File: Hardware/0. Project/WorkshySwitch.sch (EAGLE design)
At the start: 52 parts, among them IC1 LM1117-3.3, K1 G3MB-202P, Q3 32-MHz, Q4 32.768-kHz, T1 BC848, U2 HLK-PM01, U3 CC2541

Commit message: PCB layout under dev
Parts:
- removed F1: SF70E, Thermal Fuse:LITTLEFUSE
- removed IC1: LM1117-3.3, v-reg:LD117AS33TR
- added F3: SF70E, fuse:LITTLEFUSE
- added U1: LM1117-3.3, REG1117:REG1117
- X1: device con-ptr500:AK500/2-H -> con-ptr500:AK500/2
- X3: device con-ptr500:AK500/3-H -> con-ptr500:AK500/3
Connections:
- net 3.3V: now also U1.VOUT; no longer IC1.OUT
- net 5V: now also U1.VIN; no longer IC1.IN
- net GND: now also U1.GND; no longer IC1.ADJ
- net N$4: now also F3.2; no longer F1.1
- net N$9: now also F3.1; no longer F1.2
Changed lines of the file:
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@@
 <part name="GND8" library="supply1" library_urn="urn:adsk.eagle:library:371" deviceset="GND" device=""/>
 <part name="K1" library="G3MB202PDC12" deviceset="G3MB202PDC12" device="" value="G3MB-202P"/>
-<part name="IC1" library="v-reg" library_urn="urn:adsk.eagle:library:409" deviceset="LD117A?*" device="S" package3d_urn="urn:adsk.eagle:package:30370/1" technology="33TR" value="LM1117-3.3"/>
 <part name="SUPPLY8" library="supply2" library_urn="urn:adsk.eagle:library:372" deviceset="+4.1V" device="" value="5V"/>
 <part name="SUPPLY9" library="supply2" library_urn="urn:adsk.eagle:library:372" deviceset="+4.1V" device="" value="5V"/>
@@
 <part name="R4" library="rcl" library_urn="urn:adsk.eagle:library:334" deviceset="R-EU_" device="R0603" package3d_urn="urn:adsk.eagle:package:23555/3" value="1k"/>
 <part name="GND9" library="supply1" library_urn="urn:adsk.eagle:library:371" deviceset="GND" device=""/>
-<part name="X1" library="con-ptr500" library_urn="urn:adsk.eagle:library:181" deviceset="AK500/2-H" device="" package3d_urn="urn:adsk.eagle:package:9901/1"/>
+<part name="X1" library="con-ptr500" library_urn="urn:adsk.eagle:library:181" deviceset="AK500/2" device="" package3d_urn="urn:adsk.eagle:package:9880/1"/>
 <part name="GND10" library="supply1" library_urn="urn:adsk.eagle:library:371" deviceset="GND" device=""/>
 <part name="SUPPLY10" library="supply2" library_urn="urn:adsk.eagle:library:372" deviceset="+4.1V" device="" value="3.3V"/>
 <part name="F2" library="fuse" library_urn="urn:adsk.eagle:library:233" deviceset="QPL" device="" package3d_urn="urn:adsk.eagle:package:14085/1" value="200 mA"/>
-<part name="F1" library="Thermal Fuse" deviceset="LITTLEFUSE" device="" package3d_urn="urn:adsk.eagle:package:14064/1" value="SF70E"/>
 <part name="R5" library="varistor" library_urn="urn:adsk.eagle:library:410" deviceset="VARISTOR" device="S05K11" package3d_urn="urn:adsk.eagle:package:30524/1" value="130VRMS"/>
 <part name="C18" library="smd-ipc" library_urn="urn:adsk.eagle:library:361" deviceset="C0402" device="" value="18pF"/>
@@
 <part name="R2" library="smd-ipc" library_urn="urn:adsk.eagle:library:361" deviceset="R0402" device="" value="10k"/>
 <part name="R7" library="smd-ipc" library_urn="urn:adsk.eagle:library:361" deviceset="R0402" device="" value="10k"/>
-<part name="X3" library="con-ptr500" library_urn="urn:adsk.eagle:library:181" deviceset="AK500/3-H" device="" package3d_urn="urn:adsk.eagle:package:9899/1"/>
+<part name="X3" library="con-ptr500" library_urn="urn:adsk.eagle:library:181" deviceset="AK500/3" device="" package3d_urn="urn:adsk.eagle:package:9883/1"/>
+<part name="F3" library="fuse" deviceset="LITTLEFUSE" device="" package3d_urn="urn:adsk.eagle:package:14064/1" value="SF70E"/>
+<part name="U1" library="REG1117" deviceset="REG1117" device="" value="LM1117-3.3"/>
 </parts>
 <sheets>
@@
 <attribute name="VALUE" x="368.90725" y="175.874490625" size="1.274740625" layer="96"/>
 </instance>
-<instance part="IC1" gate="G$1" x="115.57" y="238.76" smashed="yes">
-<attribute name="NAME" x="110.49" y="245.11" size="1.778" layer="95"/>
-<attribute name="VALUE" x="110.49" y="242.57" size="1.4224" layer="96"/>
-</instance>
 <instance part="SUPPLY8" gate="P" x="102.87" y="243.84" smashed="yes">
 <attribute name="VALUE" x="100.965" y="247.015" size="1.778" layer="96"/>
@@
 <attribute name="NAME" x="38.1" y="242.697" size="1.778" layer="95" rot="MR0"/>
 <attribute name="VALUE" x="38.1" y="240.284" size="1.778" layer="96" rot="MR0"/>
-</instance>
-<instance part="F1" gate="A" x="46.99" y="238.76" smashed="yes" rot="MR0">
-<attribute name="NAME" x="50.8" y="242.697" size="1.778" layer="95" rot="MR0"/>
-<attribute name="VALUE" x="50.8" y="240.284" size="1.778" layer="96" rot="MR0"/>
 </instance>
 <instance part="R5" gate="G$1" x="59.69" y="233.68" smashed="yes" rot="MR90">
@@
 <attribute name="NAME" x="387.35" y="162.941" size="1.778" layer="95"/>
 <attribute name="VALUE" x="389.89" y="167.513" size="1.778" layer="96" rot="R180"/>
+</instance>
+<instance part="F3" gate="A" x="46.99" y="238.76" smashed="yes">
+<attribute name="NAME" x="43.18" y="240.157" size="1.778" layer="95"/>
+<attribute name="VALUE" x="43.18" y="235.839" size="1.778" layer="96"/>
+</instance>
+<instance part="U1" gate="G$1" x="115.57" y="237.49" smashed="yes">
+<attribute name="NAME" x="109.218809375" y="244.475890625" size="1.77828125" layer="95" ratio="10"/>
+<attribute name="VALUE" x="109.212090625" y="241.93895" size="1.778" layer="96" ratio="10"/>
 </instance>
 </instances>
@@
 <wire x1="128.27" y1="229.87" x2="128.27" y2="228.6" width="0.1524" layer="91"/>
 <junction x="128.27" y="228.6"/>
-<pinref part="IC1" gate="G$1" pin="ADJ"/>
 <wire x1="115.57" y1="231.14" x2="115.57" y2="228.6" width="0.1524" layer="91"/>
 <junction x="115.57" y="228.6"/>
@@
 <wire x1="92.71" y1="229.87" x2="92.71" y2="228.6" width="0.1524" layer="91"/>
 <junction x="92.71" y="228.6"/>
+<pinref part="U1" gate="G$1" pin="GND"/>
 </segment>
 <segment>
@@
 <net name="3.3V" class="0">
 <segment>
-<pinref part="IC1" gate="G$1" pin="OUT"/>
 <wire x1="128.27" y1="238.76" x2="128.27" y2="237.49" width="0.1524" layer="91"/>
-<wire x1="123.19" y1="238.76" x2="128.27" y2="238.76" width="0.1524" layer="91"/>
 <junction x="128.27" y="238.76"/>
 <pinref part="C1" gate="G$1" pin="1"/>
 <pinref part="C2" gate="G$1" pin="1"/>
+<wire x1="127" y1="238.76" x2="128.27" y2="238.76" width="0.1524" layer="91"/>
 <wire x1="138.43" y1="237.49" x2="138.43" y2="238.76" width="0.1524" layer="91"/>
 <wire x1="138.43" y1="238.76" x2="128.27" y2="238.76" width="0.1524" layer="91"/>
@@
 <wire x1="140.97" y1="238.76" x2="138.43" y2="238.76" width="0.1524" layer="91"/>
 <junction x="138.43" y="238.76"/>
+<pinref part="U1" gate="G$1" pin="VOUT"/>
 </segment>
 </net>
@@
 <pinref part="SUPPLY8" gate="P" pin="+4.1V"/>
 <wire x1="102.87" y1="241.3" x2="102.87" y2="238.76" width="0.1524" layer="91"/>
-<pinref part="IC1" gate="G$1" pin="IN"/>
 <wire x1="102.87" y1="238.76" x2="102.87" y2="237.49" width="0.1524" layer="91"/>
-<wire x1="107.95" y1="238.76" x2="102.87" y2="238.76" width="0.1524" layer="91"/>
 <pinref part="U2" gate="G$1" pin="VO+"/>
+<wire x1="104.14" y1="238.76" x2="102.87" y2="238.76" width="0.1524" layer="91"/>
 <wire x1="87.63" y1="238.76" x2="92.71" y2="238.76" width="0.1524" layer="91"/>
 <junction x="102.87" y="238.76"/>
@@
 <wire x1="92.71" y1="237.49" x2="92.71" y2="238.76" width="0.1524" layer="91"/>
 <junction x="92.71" y="238.76"/>
+<pinref part="U1" gate="G$1" pin="VIN"/>
 </segment>
 <segment>
@@
 <wire x1="52.07" y1="238.76" x2="59.69" y2="238.76" width="0.1524" layer="91"/>
 <wire x1="59.69" y1="238.76" x2="62.23" y2="238.76" width="0.1524" layer="91"/>
-<pinref part="F1" gate="A" pin="1"/>
+<pinref part="F3" gate="A" pin="2"/>
 </segment>
 </net>
 <net name="N$9" class="0">
 <segment>
-<pinref part="F1" gate="A" pin="2"/>
 <wire x1="39.37" y1="238.76" x2="41.91" y2="238.76" width="0.1524" layer="91"/>
 <pinref part="F2" gate="G$1" pin="1"/>
-</segment>
-</net>
+<pinref part="F3" gate="A" pin="1"/>
+</segment>
+</net>

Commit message: PCB layout done
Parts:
- removed JP2: (no value), pinhead:PINHD-2X5
- removed R3: 10k, rcl:R-EU_R0603
- removed S1: DTSM-3, switch-tact:DTSM-3
- added J1: ICSP, SHF-105-01-X-D-SM:SHF-105-01-X-D-SM
- added R1: R0402, smd-ipc:R0402
- added S2: 434121050816, Push Button:434121050816
- C1, C7: value 100nF -> (none)
- C18, C19: value 18pF -> C0402
- C2, C5: value 10uF -> (none)
- C21, C22, C24: value 1pF -> C0402
- C23: value DNM -> C0402
- C25: value 220pF -> C0402
- C26, C28, C29, C30, C31: value 100nF -> C0402
- C27, C32: value 1uF -> C0402
- C33, C34: value 12pF -> C0402
- C35, C36: value 15pF -> C0402
- C6: value 2.2uF -> C0402
- C9: value 100n -> C0402
- L1, L2: value 2nH -> L0402
- L3: value 1nH -> L0402
- L4: value 3nH -> L0402
- L5: value BLM15HG102SN1D -> L0402
- Q3: value 32-MHz -> FA-128
- Q4: value 32.768-kHz -> (none)
- R10: value 56k -> R0402
- R2, R7: value 10k -> R0402
- R4: value 1k -> R0402; device rcl:R-EU_R0603 -> smd-ipc:R0402
- R8: value 2.7k -> R0402
- U1: value LM1117-3.3 -> REG1117
- U3: value CC2541 -> CC2541F256RHAT
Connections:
- removed net +4.1V: C25.1, C26.1, C28.1, C29.1, C30.1, C31.1, C32.1, C6.1, JP2.2, L5.1, R2.2, R7.2, SJ1.2, U3.AVDD1, U3.AVDD2, U3.AVDD3, U3.AVDD4, U3.AVDD5, U3.AVDD6, U3.DVDD1, U3.DVDD2
- new net 3.3: C1.1, C2.1, L5.2, U1.VOUT
- net 3.3V: now also C25.1, C26.1, C28.1, C29.1, C30.1, C31.1, C32.1, C6.1, J1.2, L5.1, R2.2, R7.2, SJ1.2, U3.AVDD1, U3.AVDD2, U3.AVDD3, U3.AVDD4, U3.AVDD5, U3.AVDD6, U3.DVDD1, U3.DVDD2; no longer C1.1, C2.1, L5.2, U1.VOUT
- net BUTTON_PROG: now also S2.2; no longer S1.2
- net DEBUG_CLK: now also J1.3; no longer JP2.3
- net DEBUG_DATA: now also J1.4; no longer JP2.4
- net DEBUG_RESET: now also J1.7; no longer JP2.7
- net GND: now also J1.1, S2.1; no longer JP2.1, S1.1
- net LED_STATUS: now also R4.2, U3.P2_0; no longer R3.1, U3.P1_0
- net LOAD_CONTROL: now also R1.2; no longer R4.1
- net N$1: now also R4.1; no longer R3.2
- net N$10: now also J1.9; no longer JP2.9
- net N$6: now also R1.1; no longer R4.2
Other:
- moved on the sheet: R4

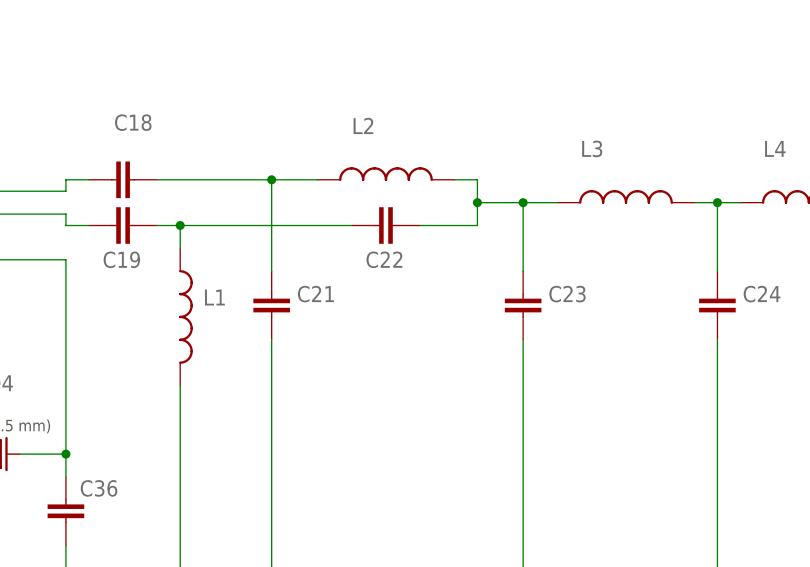
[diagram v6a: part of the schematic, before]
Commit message: 3D PCB Model Generated
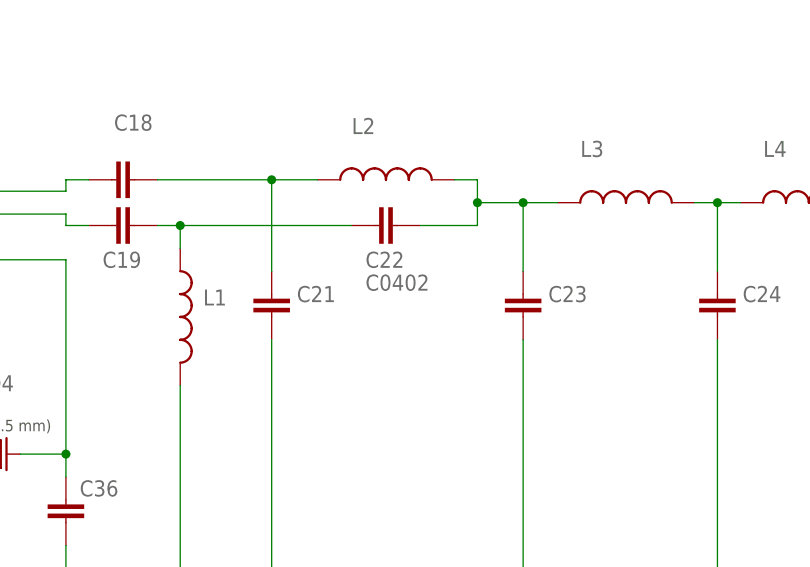
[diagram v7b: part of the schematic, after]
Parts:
- R5: device varistor:VARISTORS05K11 -> varistor:VARISTORS05K17
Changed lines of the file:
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@@
 <part name="SUPPLY10" library="supply2" library_urn="urn:adsk.eagle:library:372" deviceset="+4.1V" device="" value="3.3V"/>
 <part name="F2" library="fuse" library_urn="urn:adsk.eagle:library:233" deviceset="QPL" device="" package3d_urn="urn:adsk.eagle:package:14085/1" value="200 mA"/>
-<part name="R5" library="varistor" library_urn="urn:adsk.eagle:library:410" deviceset="VARISTOR" device="S05K11" package3d_urn="urn:adsk.eagle:package:30524/1" value="130VRMS"/>
+<part name="R5" library="varistor" library_urn="urn:adsk.eagle:library:410" deviceset="VARISTOR" device="S05K17" package3d_urn="urn:adsk.eagle:package:30525/1" value="130VRMS"/>
 <part name="C18" library="smd-ipc" library_urn="urn:adsk.eagle:library:361" deviceset="C0402" device="" value=""/>
 <part name="C19" library="smd-ipc" library_urn="urn:adsk.eagle:library:361" deviceset="C0402" device="" value=""/>
 <part name="C21" library="smd-ipc" library_urn="urn:adsk.eagle:library:361" deviceset="C0402" device="" value=""/>
-<part name="C22" library="smd-ipc" library_urn="urn:adsk.eagle:library:361" deviceset="C0402" device="" value=""/>
+<part name="C22" library="smd-ipc" library_urn="urn:adsk.eagle:library:361" deviceset="C0402" device="" value="C0402"/>
 <part name="C23" library="smd-ipc" library_urn="urn:adsk.eagle:library:361" deviceset="C0402" device="" value=""/>
 <part name="C24" library="smd-ipc" library_urn="urn:adsk.eagle:library:361" deviceset="C0402" device="" value=""/>

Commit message: Components values added
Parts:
- removed R5: 130VRMS, varistor:VARISTORS05K17
- added R3: 130VRMS, varistor:VARISTORS05K11
- C1, C7: value (none) -> 100nF
- C18, C19: value C0402 -> 18pF
- C2, C5: value (none) -> 10uF
- C21, C22, C24: value C0402 -> 1pF
- C25: value C0402 -> 220pF
- C26, C28, C29, C30, C31: value C0402 -> 100nF
- C27, C32: value C0402 -> 1uF
- C33, C34: value C0402 -> 12pF
- C35, C36: value C0402 -> 15pF
- C6: value C0402 -> 2.2uF
- C9: value C0402 -> 1nF
- L1, L2: value L0402 -> 2nH
- L3: value L0402 -> 1nH
- L4: value L0402 -> 3nH
- L5: value L0402 -> Ferrite Bead
- LED1: value (none) -> Green
- Q3: value FA-128 -> 32-MHz
- Q4: value (none) -> 32-kHz
- R1: value R0402 -> 1k
- R10: value R0402 -> 56k
- R2, R7: value R0402 -> 10k
- R4: value R0402 -> 4.7k
- R8: value R0402 -> 2.7k
- SJ1: value (none) -> Jumper
- U1: value REG1117 -> LM1117-3.3
- U3: value CC2541F256RHAT -> CC2541
- X1: value (none) -> Therminal Block 2 Vias
- X3: value (none) -> Therminal Bloc 3 Vias
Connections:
- net N$3: now also R3.2; no longer R5.2
- net N$4: now also R3.1; no longer R5.1
